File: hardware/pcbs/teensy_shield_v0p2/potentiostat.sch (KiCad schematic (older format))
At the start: 137 parts, among them K1 Conn_01x03, P1 Conn_01x02, P10 Conn_01x02, P11 Conn_01x02, P12 Conn_01x02, P13 Conn_02x05_Odd_Even, P14 Conn_02x05_Odd_Even, P15 Conn_02x02_Odd_Even, P16 Conn_02x02_Odd_Even, P17 Conn_01x02, P18 Conn_01x02, P19 Conn_01x02, P2 Conn_01x02, P20 Conn_01x02, P21 Conn_01x02, P22 Conn_01x02, P3 Conn_01x02, P4 Conn_01x02, P5 Conn_01x02, P6 Conn_01x02, P7 Conn_01x02, P8 Conn_01x02, P9 Conn_01x02, U1 74HC138, U10 REF33XX, U11 OP07, U12 OP07, U13 OP07, U14 OP07, U15 OP07, U16 OP07, U17 OP07, U18 OP07, U19 74HC138, U2 TEENSY3.1, U20 OP07, U21 74HC138, U3 DG411xY, U4 DG411xY, U5 DG411xY, U6 MEA1D05XXSC, U7 DG411xY, U8 DG411xY, U9 TL072

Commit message: Added new BOMs.
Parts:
- C1, C5: LCSC Part (none) -> C19666
- C25, C26, C27, C28: value 56nF -> 68nF
- D1, D2: LCSC Part (none) -> C609810
- U1, U19, U21: LCSC Part (none) -> C5602
- U10: LCSC Part (none) -> C140329
- U11, U13, U15, U16, U17, U18, U20: LCSC Part (none) -> C7433
- U3, U4, U5, U7, U8: LCSC Part (none) -> C17218
- U9: LCSC Part (none) -> C6961
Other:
- note removed: "3V reference \nLCSC#: C140329\nREF3330AIDBZR"
- note removed: "LCSC#: C17218"
- note removed: "LCSC#: C5602"
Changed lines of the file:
@@
 F 2 "Package_SO:SOIC-8_3.9x4.9mm_P1.27mm" H 3100 8075 50  0001 C CNN
 F 3 "https://www.analog.com/media/en/technical-documentation/data-sheets/OP07.pdf" H 3100 8175 50  0001 C CNN
+F 4 "C7433" H 3050 8025 50  0001 C CNN "LCSC Part"
 	1    3050 8025
 	1    0    0    1
@@
 F 2 "Package_SO:SOIC-16_3.9x9.9mm_P1.27mm" H 2175 5625 50  0001 C CNN
 F 3 "http://www.ti.com/lit/ds/symlink/cd74hc238.pdf" H 2175 5625 50  0001 C CNN
+F 4 "C5602" H 2175 5625 50  0001 C CNN "LCSC Part"
 	1    2175 5625
 	1    0    0    -1
@@
 F 2 "Package_SO:SOIC-8_3.9x4.9mm_P1.27mm" H 5250 8175 50  0001 C CNN
 F 3 "https://www.analog.com/media/en/technical-documentation/data-sheets/OP07.pdf" H 5250 8275 50  0001 C CNN
+F 4 "C7433" H 5200 8125 50  0001 C CNN "LCSC Part"
 	1    5200 8125
 	1    0    0    1
@@
 F 2 "Package_SO:SOIC-16_3.9x9.9mm_P1.27mm" H 3900 5600 50  0001 C CNN
 F 3 "https://datasheets.maximintegrated.com/en/ds/DG411-DG413.pdf" H 3900 5700 50  0001 C CNN
+F 4 "C17218" H 3900 5700 50  0001 C CNN "LCSC Part"
 	5    3900 5700
 	1    0    0    -1
@@
 Wire Wire Line
 	3900 8025 4150 8025
-Text Notes 4300 5375 3    60   ~ 0
-LCSC#: C17218
-Text Notes 2750 5625 3    60   ~ 0
-LCSC#: C5602
 Text Notes 1800 7350 0    50   ~ 0
 OP07\nLCSC# C7433
@@
 F 2 "Capacitor_SMD:C_0603_1608Metric" H 1338 10950 50  0001 C CNN
 F 3 "~" H 1300 11100 50  0001 C CNN
+F 4 "C19666" H 1300 11100 50  0001 C CNN "LCSC Part"
 	1    1300 11100
 	1    0    0    -1
@@
 F 2 "Capacitor_SMD:C_0603_1608Metric" H 2538 11300 50  0001 C CNN
 F 3 "~" H 2500 11450 50  0001 C CNN
+F 4 "C19666" H 2500 11450 50  0001 C CNN "LCSC Part"
 	1    2500 11450
 	1    0    0    -1
@@
 F 2 "Package_SO:SOIC-8_3.9x4.9mm_P1.27mm" H 3800 11250 50  0001 C CNN
 F 3 "https://www.analog.com/media/en/technical-documentation/data-sheets/OP07.pdf" H 3800 11350 50  0001 C CNN
+F 4 "" H 3750 11200 50  0001 C CNN "LCSC Part"
 	1    3750 11200
 	1    0    0    1
@@
 Wire Wire Line
 	2500 11100 2500 10800
-Text Notes 1550 11775 0    60   ~ 0
-3V reference \nLCSC#: C140329\nREF3330AIDBZR
 Text Notes 650  -1300 0    200  ~ 0
 Notes:\n\n1.) Don't forget the bypass capacitors!!!\n2.) Maybe change DC converter from  +/-15V  to +/-15V \n3.) Add switch to working electrode ( and counter and reference?)\n4.) Add low pass filters to inputs  (DAC) and outputs (ADC)\n
@@
 F 2 "Package_SO:SOIC-8_3.9x4.9mm_P1.27mm" H 15200 8675 50  0001 C CNN
 F 3 "https://www.analog.com/media/en/technical-documentation/data-sheets/OP07.pdf" H 15200 8775 50  0001 C CNN
+F 4 "C7433" H 15150 8625 50  0001 C CNN "LCSC Part"
 	1    15150 8625
 	1    0    0    1
@@
 F 2 "Package_SO:SOIC-16_3.9x9.9mm_P1.27mm" H 20625 8675 50  0001 C CNN
 F 3 "http://www.ti.com/lit/ds/symlink/cd74hc238.pdf" H 20625 8675 50  0001 C CNN
+F 4 "C5602" H 20625 8675 50  0001 C CNN "LCSC Part"
 	1    20625 8675
 	1    0    0    -1
@@
 F 2 "Package_SO:SOIC-8_3.9x4.9mm_P1.27mm" H 15275 13175 50  0001 C CNN
 F 3 "https://www.analog.com/media/en/technical-documentation/data-sheets/OP07.pdf" H 15275 13275 50  0001 C CNN
+F 4 "C7433" H 15225 13125 50  0001 C CNN "LCSC Part"
 	1    15225 13125
 	1    0    0    1
@@
 F 2 "Package_SO:SOIC-16_3.9x9.9mm_P1.27mm" H 18050 8450 50  0001 C CNN
 F 3 "https://datasheets.maximintegrated.com/en/ds/DG411-DG413.pdf" H 18050 8550 50  0001 C CNN
+F 4 "C17218" V 18050 8550 50  0001 C CNN "LCSC Part"
 	5    18050 8550
 	1    0    0    -1
@@
 F 2 "Package_SO:SOIC-8_3.9x4.9mm_P1.27mm" H 18425 13275 50  0001 C CNN
 F 3 "https://www.analog.com/media/en/technical-documentation/data-sheets/OP07.pdf" H 18425 13375 50  0001 C CNN
+F 4 "C7433" H 18375 13225 50  0001 C CNN "LCSC Part"
 	1    18375 13225
 	1    0    0    1
@@
 F 2 "Package_TO_SOT_SMD:SOT-23" H 1900 11100 50  0001 C CNN
 F 3 "" H 1900 11100 50  0001 C CNN
+F 4 "C140329" H 1900 11100 50  0001 C CNN "LCSC Part"
 	1    1900 11100
 	1    0    0    -1
@@
 F 2 "Package_SO:SOIC-8_3.9x4.9mm_P1.27mm" H 6000 11350 50  0001 C CNN
 F 3 "https://www.analog.com/media/en/technical-documentation/data-sheets/OP07.pdf" H 6000 11450 50  0001 C CNN
+F 4 "" H 5950 11300 50  0001 C CNN "LCSC Part"
 	1    5950 11300
 	1    0    0    1
@@
 F 2 "Package_TO_SOT_SMD:SOT-23" H 19975 12825 60  0001 C CNN
 F 3 "~" H 19975 12825 60  0000 C CNN
+F 4 "C609810 " H 19975 12825 50  0001 C CNN "LCSC Part"
 	1    19975 12825
 	1    0    0    -1
@@
 F 2 "Package_SO:SOIC-8_3.9x4.9mm_P1.27mm" H 13125 5500 50  0001 C CNN
 F 3 "http://www.ti.com/lit/ds/symlink/tl071.pdf" H 13125 5500 50  0001 C CNN
+F 4 "C6961" H 13125 5500 50  0001 C CNN "LCSC Part"
 	1    13125 5500
 	1    0    0    1
@@
 F 2 "Package_SO:SOIC-8_3.9x4.9mm_P1.27mm" H 12700 9125 50  0001 C CNN
 F 3 "http://www.ti.com/lit/ds/symlink/tl071.pdf" H 12700 9125 50  0001 C CNN
+F 4 "C6961" H 12700 9125 50  0001 C CNN "LCSC Part"
 	2    12700 9125
 	1    0    0    1
@@
 F 2 "Package_SO:SOIC-16_3.9x9.9mm_P1.27mm" H 22625 2525 50  0001 C CNN
 F 3 "http://www.ti.com/lit/ds/symlink/cd74hc238.pdf" H 22625 2525 50  0001 C CNN
+F 4 "C5602" H 22625 2525 50  0001 C CNN "LCSC Part"
 	1    22625 2525
 	-1   0    0    -1
@@
 P 13175 1350
 F 0 "C25" V 13075 1200 50  0000 C CNN
-F 1 "56nF" V 13075 1500 50  0000 C CNN
+F 1 "68nF" V 13075 1500 50  0000 C CNN
 F 2 "Capacitor_SMD:C_0603_1608Metric" H 13213 1200 50  0001 C CNN
 F 3 "~" H 13175 1350 50  0001 C CNN
@@
 P 13225 4700
 F 0 "C28" V 13125 4550 50  0000 C CNN
-F 1 "56nF" V 13125 4850 50  0000 C CNN
+F 1 "68nF" V 13125 4850 50  0000 C CNN
 F 2 "Capacitor_SMD:C_0603_1608Metric" H 13263 4550 50  0001 C CNN
 F 3 "~" H 13225 4700 50  0001 C CNN
@@
 P 13175 2500
 F 0 "C26" V 13075 2350 50  0000 C CNN
-F 1 "56nF" V 13075 2650 50  0000 C CNN
+F 1 "68nF" V 13075 2650 50  0000 C CNN
 F 2 "Capacitor_SMD:C_0603_1608Metric" H 13213 2350 50  0001 C CNN
 F 3 "~" H 13175 2500 50  0001 C CNN
@@
 P 13175 3650
 F 0 "C27" V 13075 3500 50  0000 C CNN
-F 1 "56nF" V 13075 3800 50  0000 C CNN
+F 1 "68nF" V 13075 3800 50  0000 C CNN
 F 2 "Capacitor_SMD:C_0603_1608Metric" H 13213 3500 50  0001 C CNN
 F 3 "~" H 13175 3650 50  0001 C CNN
@@
 F 2 "Package_SO:SOIC-16_3.9x9.9mm_P1.27mm" H 19875 2300 50  0001 C CNN
 F 3 "https://datasheets.maximintegrated.com/en/ds/DG411-DG413.pdf" H 19875 2400 50  0001 C CNN
+F 4 "C17218" H 19875 2400 50  0001 C CNN "LCSC Part"
 	5    19875 2400
 	1    0    0    -1
@@
 F 2 "Package_SO:SOIC-16_3.9x9.9mm_P1.27mm" H 18850 2325 50  0001 C CNN
 F 3 "https://datasheets.maximintegrated.com/en/ds/DG411-DG413.pdf" H 18850 2425 50  0001 C CNN
+F 4 "C17218" H 18850 2425 50  0001 C CNN "LCSC Part"
 	5    18850 2425
 	1    0    0    -1
@@
 F 2 "Package_SO:SOIC-8_3.9x4.9mm_P1.27mm" H 21975 5750 50  0001 C CNN
 F 3 "https://www.analog.com/media/en/technical-documentation/data-sheets/OP07.pdf" H 21975 5850 50  0001 C CNN
+F 4 "C7433" H 21925 5700 50  0001 C CNN "LCSC Part"
 	1    21925 5700
 	1    0    0    1
@@
 F 2 "Package_TO_SOT_SMD:SOT-23" H 23525 5300 60  0001 C CNN
 F 3 "~" H 23525 5300 60  0000 C CNN
+F 4 "C609810 " H 23525 5300 50  0001 C CNN "LCSC Part"
 	1    23525 5300
 	1    0    0    -1
@@
 F 2 "Package_SO:SOIC-8_3.9x4.9mm_P1.27mm" H 19150 5650 50  0001 C CNN
 F 3 "https://www.analog.com/media/en/technical-documentation/data-sheets/OP07.pdf" H 19150 5750 50  0001 C CNN
+F 4 "C7433" H 19100 5600 50  0001 C CNN "LCSC Part"
 	1    19100 5600
 	1    0    0    1
@@
 F 2 "Package_SO:SOIC-16_3.9x9.9mm_P1.27mm" H 1700 14125 50  0001 C CNN
 F 3 "https://datasheets.maximintegrated.com/en/ds/DG411-DG413.pdf" H 1700 14225 50  0001 C CNN
+F 4 "C17218" H 1700 14225 50  0001 C CNN "LCSC Part"
 	5    1700 14225
 	1    0    0    -1

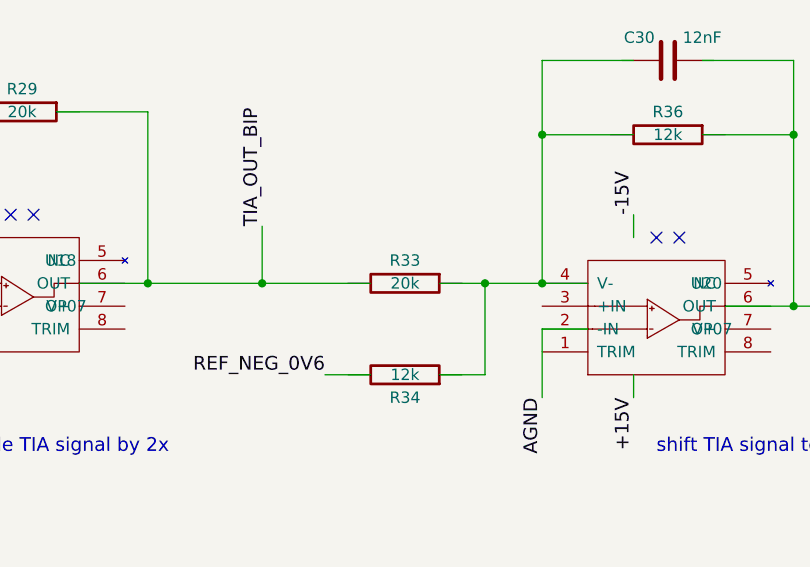
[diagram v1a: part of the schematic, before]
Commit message: Modified R33 resistor value which caused gain error, for transimpedance amplifier in first prototypes of V0.2 design.
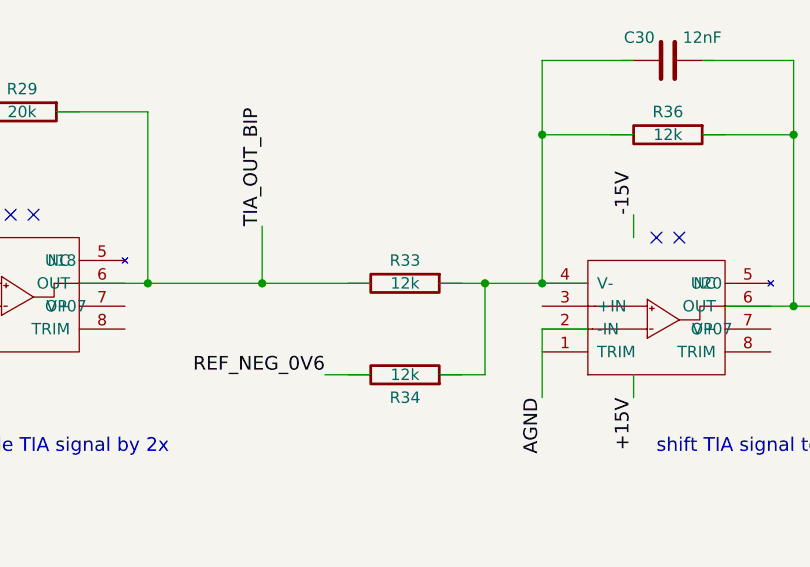
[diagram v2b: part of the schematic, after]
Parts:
- R33: value 20k -> 12k
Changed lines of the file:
@@
 P 20825 5600
 F 0 "R33" V 20725 5600 50  0000 C CNN
-F 1 "20k" V 20825 5600 50  0000 C CNN
+F 1 "12k" V 20825 5600 50  0000 C CNN
 F 2 "Resistor_SMD:R_0603_1608Metric" V 20755 5600 50  0001 C CNN
 F 3 "~" H 20825 5600 50  0001 C CNN

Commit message: Fixed footprint issue with mx design.
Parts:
- P1, P2, P3: footprint pin_array:PIN_ARRAY_2X1 -> ost_connblocks:CONNBLOCK2
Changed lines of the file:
@@
 F 0 "P1" H 8530 13442 50  0000 L CNN
 F 1 "Conn_01x02" H 8530 13351 50  0000 L CNN
-F 2 "pin_array:PIN_ARRAY_2X1" H 8450 13450 50  0001 C CNN
+F 2 "ost_connblocks:CONNBLOCK2" H 8450 13450 50  0001 C CNN
 F 3 "~" H 8450 13450 50  0001 C CNN
 	1    8450 13450
@@
 F 0 "P2" H 8530 14392 50  0000 L CNN
 F 1 "Conn_01x02" H 8530 14301 50  0000 L CNN
-F 2 "pin_array:PIN_ARRAY_2X1" H 8450 14400 50  0001 C CNN
+F 2 "ost_connblocks:CONNBLOCK2" H 8450 14400 50  0001 C CNN
 F 3 "~" H 8450 14400 50  0001 C CNN
 	1    8450 14400
@@
 F 0 "P3" H 8530 15392 50  0000 L CNN
 F 1 "Conn_01x02" H 8530 15301 50  0000 L CNN
-F 2 "pin_array:PIN_ARRAY_2X1" H 8450 15400 50  0001 C CNN
+F 2 "ost_connblocks:CONNBLOCK2" H 8450 15400 50  0001 C CNN
 F 3 "~" H 8450 15400 50  0001 C CNN
 	1    8450 15400
